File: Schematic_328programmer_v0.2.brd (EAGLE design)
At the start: 53.9 x 54.3 mm, 15 parts, among them IC1 ATTiny85, U1 ATMEGA328P_TQFP, Y1 16mhz

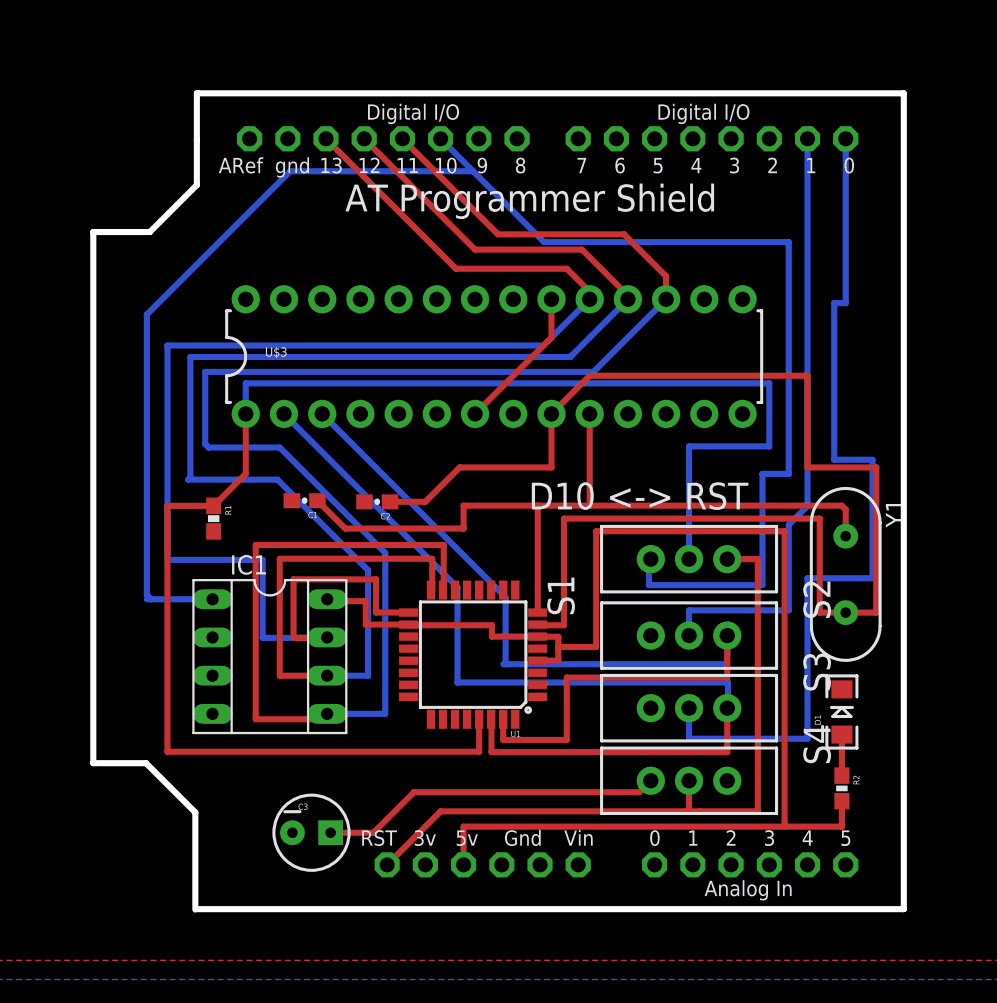
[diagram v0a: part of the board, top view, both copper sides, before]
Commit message: Updated Board CAD files
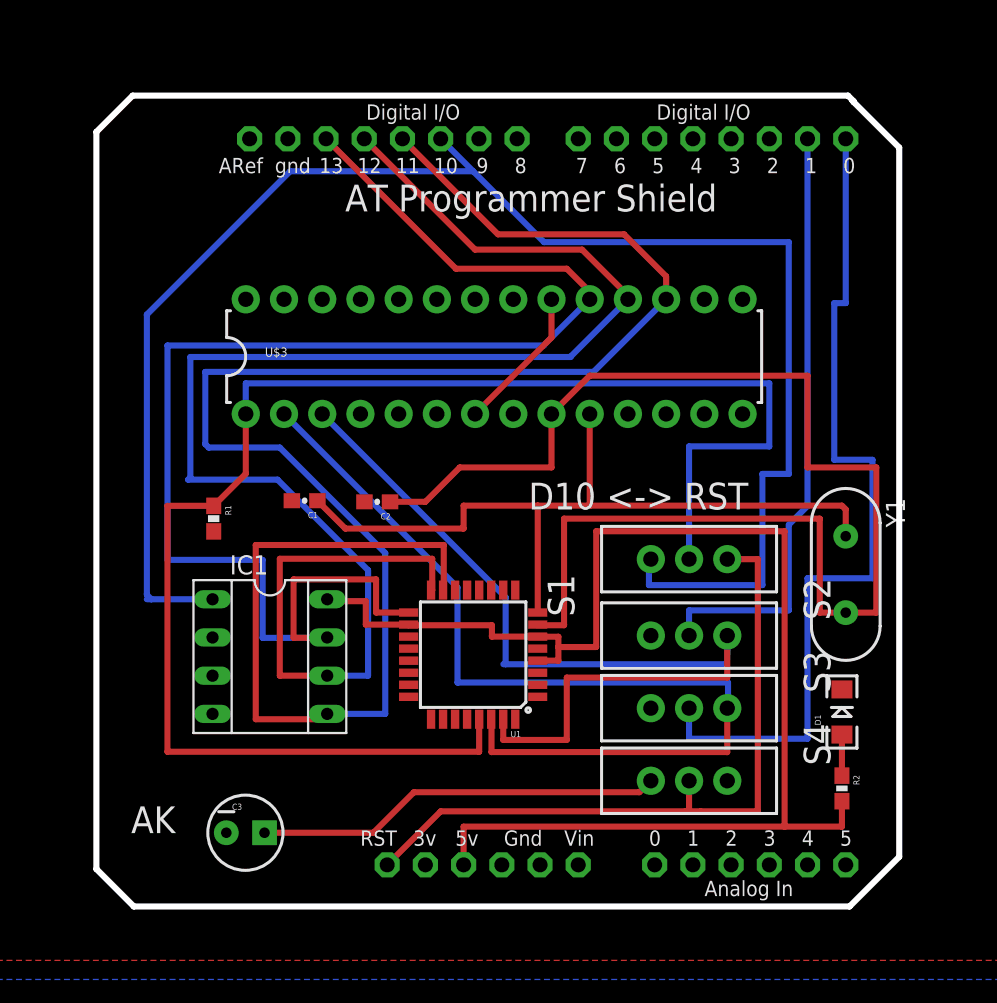
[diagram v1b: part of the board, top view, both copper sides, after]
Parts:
- moved C3 4.39 mm to (29.9, 5.94)
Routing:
- net N$5: track 22.7 -> 27.1 mm
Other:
- board size 53.9 x 54.3 mm -> 53.4 x 53.9 mm
- board text added: "AK"
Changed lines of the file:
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@@
 <text x="48.768" y="27.432" size="1.778" layer="21">D10 &lt;-&gt; RST</text>
 <text x="36.576" y="47.244" size="1.778" layer="21">AT Programmer Shield</text>
-<wire x1="26.7716" y1="0.8636" x2="73.7108" y2="0.8636" width="0.4064" layer="20"/>
-<wire x1="73.7108" y1="0.8636" x2="73.7108" y2="55.0926" width="0.4064" layer="20"/>
-<wire x1="73.7108" y1="55.0926" x2="26.8478" y2="55.0926" width="0.4064" layer="20"/>
-<wire x1="26.6192" y1="0.8382" x2="26.6192" y2="7.2898" width="0.4064" layer="20"/>
-<wire x1="26.6192" y1="7.2898" x2="23.3426" y2="10.5664" width="0.4064" layer="20"/>
-<wire x1="23.3426" y1="10.5664" x2="19.8374" y2="10.5664" width="0.4064" layer="20"/>
-<wire x1="19.8374" y1="10.5664" x2="19.8374" y2="45.8724" width="0.4064" layer="20"/>
-<wire x1="19.8374" y1="45.8724" x2="23.5966" y2="45.8724" width="0.4064" layer="20"/>
-<wire x1="23.5966" y1="45.8724" x2="26.7208" y2="48.9966" width="0.4064" layer="20"/>
-<wire x1="26.7208" y1="48.9966" x2="26.7208" y2="51.943" width="0.4064" layer="20"/>
-<wire x1="26.7208" y1="51.943" x2="26.7208" y2="51.9684" width="0.4064" layer="20"/>
-<wire x1="26.797" y1="55.0926" x2="26.7208" y2="55.0926" width="0.4064" layer="20"/>
-<wire x1="26.7208" y1="55.0926" x2="26.7208" y2="51.9684" width="0.4064" layer="20"/>
+<wire x1="70.2818" y1="54.61" x2="70.3834" y2="54.5084" width="0.4064" layer="20"/>
+<wire x1="70.3834" y1="54.5084" x2="73.406" y2="51.4858" width="0.4064" layer="20"/>
+<wire x1="73.406" y1="51.4858" x2="73.406" y2="4.3434" width="0.4064" layer="20"/>
+<wire x1="73.406" y1="4.3434" x2="70.104" y2="1.0414" width="0.4064" layer="20"/>
+<wire x1="70.104" y1="1.0414" x2="22.5298" y2="1.0414" width="0.4064" layer="20"/>
+<wire x1="22.5298" y1="1.0414" x2="20.0406" y2="3.5306" width="0.4064" layer="20"/>
+<wire x1="20.0406" y1="3.5306" x2="20.0406" y2="52.5272" width="0.4064" layer="20"/>
+<wire x1="20.0406" y1="52.5272" x2="22.4536" y2="54.9402" width="0.4064" layer="20"/>
+<wire x1="22.4536" y1="54.9402" x2="70.0024" y2="54.9402" width="0.4064" layer="20"/>
+<wire x1="70.0024" y1="54.9402" x2="70.3834" y2="54.5592" width="0.4064" layer="20"/>
+<wire x1="70.3834" y1="54.5592" x2="70.3834" y2="54.5084" width="0.4064" layer="20"/>
+<text x="22.352" y="5.9182" size="1.778" layer="21" font="vector">AK</text>
 </plain>
 <attributes>
@@
 </class>
 </classes>
-<designrules name="default">
+<designrules name="LaenPCBOrder">
 <description language="de">&lt;b&gt;EAGLE Design Rules&lt;/b&gt;
 &lt;p&gt;
@@
 Einstellungen hier und speichern die Design Rules unter
 einem neuen Namen ab.</description>
-<description language="en">&lt;b&gt;EAGLE Design Rules&lt;/b&gt;
+<description language="en">&lt;b&gt;Laen's PCB Order Design Rules&lt;/b&gt;
 &lt;p&gt;
-The default Design Rules have been set to cover
-a wide range of applications. Your particular design
-may have different requirements, so please make the
-necessary adjustments and save your customized
-design rules under a new name.</description>
+Please make sure your boards conform to these design rules.</description>
 <param name="layerSetup" value="(1*16)"/>
-<param name="mtCopper" value="0.035mm 0.035mm 0.035mm 0.035mm 0.035mm 0.035mm 0.035mm 0.035mm 0.035mm 0.035mm 0.035mm 0.035mm 0.035mm 0.035mm 0.035mm 0.035mm"/>
-<param name="mtIsolate" value="1.5mm 0.15mm 0.2mm 0.15mm 0.2mm 0.15mm 0.2mm 0.15mm 0.2mm 0.15mm 0.2mm 0.15mm 0.2mm 0.15mm 0.2mm"/>
-<param name="mdWireWire" value="8mil"/>
-<param name="mdWirePad" value="8mil"/>
-<param name="mdWireVia" value="8mil"/>
-<param name="mdPadPad" value="8mil"/>
-<param name="mdPadVia" value="8mil"/>
-<param name="mdViaVia" value="8mil"/>
-<param name="mdSmdPad" value="8mil"/>
-<param name="mdSmdVia" value="8mil"/>
-<param name="mdSmdSmd" value="8mil"/>
+<param name="mtCopper" value="0.0356mm 0.0356mm 0.0356mm 0.0356mm 0.0356mm 0.0356mm 0.0356mm 0.0356mm 0.0356mm 0.0356mm 0.0356mm 0.0356mm 0.0356mm 0.0356mm 0.0356mm 0.0356mm"/>
+<param name="mtIsolate" value="1.5011mm 0.1499mm 0.2007mm 0.1499mm 0.2007mm 0.1499mm 0.2007mm 0.1499mm 0.2007mm 0.1499mm 0.2007mm 0.1499mm 0.2007mm 0.1499mm 0.2007mm"/>
+<param name="mdWireWire" value="6mil"/>
+<param name="mdWirePad" value="6mil"/>
+<param name="mdWireVia" value="6mil"/>
+<param name="mdPadPad" value="6mil"/>
+<param name="mdPadVia" value="6mil"/>
+<param name="mdViaVia" value="6mil"/>
+<param name="mdSmdPad" value="6mil"/>
+<param name="mdSmdVia" value="6mil"/>
+<param name="mdSmdSmd" value="6mil"/>
 <param name="mdViaViaSameLayer" value="8mil"/>
 <param name="mnLayersViaInSmd" value="2"/>
-<param name="mdCopperDimension" value="40mil"/>
-<param name="mdDrill" value="8mil"/>
+<param name="mdCopperDimension" value="15mil"/>
+<param name="mdDrill" value="6mil"/>
 <param name="mdSmdStop" value="0mil"/>
-<param name="msWidth" value="10mil"/>
-<param name="msDrill" value="24mil"/>
-<param name="msMicroVia" value="9.99mm"/>
+<param name="msWidth" value="6mil"/>
+<param name="msDrill" value="13mil"/>
+<param name="msMicroVia" value="13mil"/>
 <param name="msBlindViaRatio" value="0.5"/>
 <param name="rvPadTop" value="0.25"/>
@@
 <param name="rvMicroViaOuter" value="0.25"/>
 <param name="rvMicroViaInner" value="0.25"/>
-<param name="rlMinPadTop" value="10mil"/>
+<param name="rlMinPadTop" value="7mil"/>
 <param name="rlMaxPadTop" value="20mil"/>
-<param name="rlMinPadInner" value="10mil"/>
+<param name="rlMinPadInner" value="7mil"/>
 <param name="rlMaxPadInner" value="20mil"/>
-<param name="rlMinPadBottom" value="10mil"/>
+<param name="rlMinPadBottom" value="7mil"/>
 <param name="rlMaxPadBottom" value="20mil"/>
-<param name="rlMinViaOuter" value="8mil"/>
+<param name="rlMinViaOuter" value="7mil"/>
 <param name="rlMaxViaOuter" value="20mil"/>
-<param name="rlMinViaInner" value="8mil"/>
+<param name="rlMinViaInner" value="7mil"/>
 <param name="rlMaxViaInner" value="20mil"/>
 <param name="rlMinMicroViaOuter" value="4mil"/>
@@
 <param name="mvStopFrame" value="1"/>
 <param name="mvCreamFrame" value="0"/>
-<param name="mlMinStopFrame" value="4mil"/>
-<param name="mlMaxStopFrame" value="4mil"/>
+<param name="mlMinStopFrame" value="3mil"/>
+<param name="mlMaxStopFrame" value="3mil"/>
 <param name="mlMinCreamFrame" value="0mil"/>
 <param name="mlMaxCreamFrame" value="0mil"/>
@@
 <attribute name="PROD_ID" value="SWCH-08261" x="59.436" y="9.398" size="1.778" layer="27" rot="R270" display="off"/>
 </element>
-<element name="C3" library="SparkFun-Capacitors" package="CPOL-RADIAL-10UF-25V" value="10uF" x="34.3408" y="5.9436">
-<attribute name="PROD_ID" value="CAP-08440" x="34.3408" y="5.9436" size="1.778" layer="27" display="off"/>
+<element name="C3" library="SparkFun-Capacitors" package="CPOL-RADIAL-10UF-25V" value="10uF" x="29.9466" y="5.9436">
+<attribute name="PROD_ID" value="CAP-08440" x="29.9466" y="5.9436" size="1.778" layer="27" display="off"/>
 </element>
 </elements>
@@
 <wire x1="56.134" y1="8.636" x2="41.148" y2="8.636" width="0.4064" layer="1"/>
 <wire x1="41.148" y1="8.636" x2="38.4556" y2="5.9436" width="0.4064" layer="1"/>
-<wire x1="38.4556" y1="5.9436" x2="35.6108" y2="5.9436" width="0.4064" layer="1"/>
+<wire x1="38.4556" y1="5.9436" x2="31.2166" y2="5.9436" width="0.4064" layer="1"/>
 </signal>
 </signals>
